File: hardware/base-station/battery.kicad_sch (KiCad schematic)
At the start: 24 parts, among them J2 USB4110GFA, U13 NTMD6N02R2G, U14 MAX17303G+, U5 BQ21040DBVR

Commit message: hardware: BOM-cost pass across all four boards
Component changes from a cross-board cost review. Per-board component cost
(USD @~100qty): rocket $86.21 -> $61.39, base station $35.91 -> $29.89, with
the LoRa daughterboard and GNSS SAM-M10Q board added to the shared BOM.

Memory architecture
  - Rocket: MR25H10 MRAM deleted; the log ring moves to in-package PSRAM.
    ESP32-S3 -> ESP32-S3RH2 (2 MB quad PSRAM, no in-package flash, same land
    pattern; SPICS1/GPIO26 was already unconnected on every board).
    Persistence across boots is knowingly given up.
  - Rocket NAND F35SQB004G-WWT -> GD5F2GQ5UEYIGR: pin- and footprint-identical
    (verified against the U11 land pattern), 4 Gbit -> 2 Gbit, $11.61 -> $3.50.
    Needs the 4096 -> 2048 B page migration in firmware.
  - Base station: dedicated log flash deleted entirely. It wrote one ~183 B CSV
    row per received packet at the 2 Hz downlink (~366 B/s, and only while a
    flight is active), so 256 MB was ~204 hours of headroom. The firmware
    already falls back to the existing SPIFFS partition, so this promotes a
    tested path rather than needing new code.
  - Boot flash W25Q64JVXGIQ -> W25Q128JVSIQ on all four positions: 16 MB for
    LESS money ($3.10 -> $2.21). SCHEMATIC ONLY - the boards still need
    "Update PCB from Schematic" plus re-placement, since SOIC-8 208mil is 2.2x
    the DFN's area. The DFN's 9th (exposed) pad was a redundant GND tie; pin 4
    is GND on all four, so nothing is lost.

Power
  - LoRa + GNSS keep TPS62913 (low-noise, RF rails). The rocket briefly moved
    to it and was REVERTED to TPS62152: the TPS62913 is forced-PWM with 5 mA
    quiescent, which would have raised the pad-idle floor ~6x against the
    light-sleep work.
  - Base load switch TPS22810 -> TPS22918 (identical footprint and pin order;
    pin 3 EN/UVLO -> ON is safe because it was driven as a plain enable).
    CT cap 10 nF -> 2.2 nF to match the rocket's ramp; R8 (QOD->VOUT) deleted.
  - LoRa gains a 7.5k S-CONF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
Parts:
- removed JP1: SolderJumper_2_Open, Jumper:SolderJumper-2_P1.3mm_Open_Pad1.0x1.5mm, symbol Jumper:SolderJumper_2_Open
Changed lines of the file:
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@@
 	)
 	(junction
-		(at 145.415 118.745)
-		(diameter 0)
-		(color 0 0 0 0)
-	)
-	(junction
 		(at 154.305 73.025)
 		(diameter 0)
@@
 	(wire
 		(pts
-			(xy 194.945 106.045) (xy 172.72 106.045)
-		)
-		(stroke
-			(width 0)
-			(type default)
-		)
-	)
-	(wire
-		(pts
 			(xy 107.315 157.48) (xy 84.455 157.48)
 		)
@@
 	(wire
 		(pts
-			(xy 67.31 118.745) (xy 145.415 118.745)
+			(xy 67.31 118.745) (xy 147.32 118.745)
 		)
 		(stroke
@@
 	(wire
 		(pts
-			(xy 145.415 118.745) (xy 147.32 118.745)
-		)
-		(stroke
-			(width 0)
-			(type default)
-		)
-	)
-	(wire
-		(pts
 			(xy 79.375 181.61) (xy 67.31 181.61)
 		)
@@
 	(wire
 		(pts
-			(xy 145.415 106.045) (xy 165.1 106.045)
-		)
-		(stroke
-			(width 0)
-			(type default)
-		)
-	)
-	(wire
-		(pts
-			(xy 194.945 106.045) (xy 194.945 118.745)
-		)
-		(stroke
-			(width 0)
-			(type default)
-		)
-	)
-	(wire
-		(pts
 			(xy 90.17 177.165) (xy 90.17 181.61)
 		)
@@
 	(wire
 		(pts
-			(xy 145.415 106.045) (xy 145.415 118.745)
-		)
-		(stroke
-			(width 0)
-			(type default)
-		)
-	)
-	(wire
-		(pts
 			(xy 154.305 50.165) (xy 167.64 50.165)
 		)
@@
 					(unit 1)
 				)
-			)
-		)
-	)
-	(symbol
-		(lib_id "Jumper:SolderJumper_2_Open")
-		(at 168.91 106.045 0)
-		(unit 1)
-		(body_style 1)
-		(exclude_from_sim no)
-		(in_bom no)
-		(on_board yes)
-		(in_pos_files yes)
-		(dnp no)
-		(fields_autoplaced yes)
-		(property "Reference" "JP1"
-			(at 168.91 99.695 0)
-			(show_name no)
-			(do_not_autoplace no)
-			(effects
-				(font
-					(size 1.27 1.27)
-				)
-			)
-		)
-		(property "Value" "SolderJumper_2_Open"
-			(at 168.91 102.235 0)
-			(show_name no)
-			(do_not_autoplace no)
-			(effects
-				(font
-					(size 1.27 1.27)
-				)
-			)
-		)
-		(property "Footprint" "Jumper:SolderJumper-2_P1.3mm_Open_Pad1.0x1.5mm"
-			(at 168.91 106.045 0)
-			(hide yes)
-			(show_name no)
-			(do_not_autoplace no)
-			(effects
-				(font
-					(size 1.27 1.27)
-				)
-			)
-		)
-		(property "Datasheet" ""
-			(at 168.91 106.045 0)
-			(hide yes)
-			(show_name no)
-			(do_not_autoplace no)
-			(effects
-				(font
-					(size 1.27 1.27)
-				)
-			)
-		)
-		(property "Description" "Solder Jumper, 2-pole, open"
-			(at 168.91 106.045 0)
-			(hide yes)
-			(show_name no)
-			(do_not_autoplace no)
-			(effects
-				(font
-					(size 1.27 1.27)
-				)
-			)
-		)
-		(pin "1"
-		)
-		(pin "2"
-		)
-		(instances
-			(project "base-station"
-				(path "/d2421514-d142-4c71-ac69-48d30c1a771f/2379f198-28b9-4984-b470-63cb7f5b1a0e"
-					(reference "JP1")
-					(unit 1)
-				)

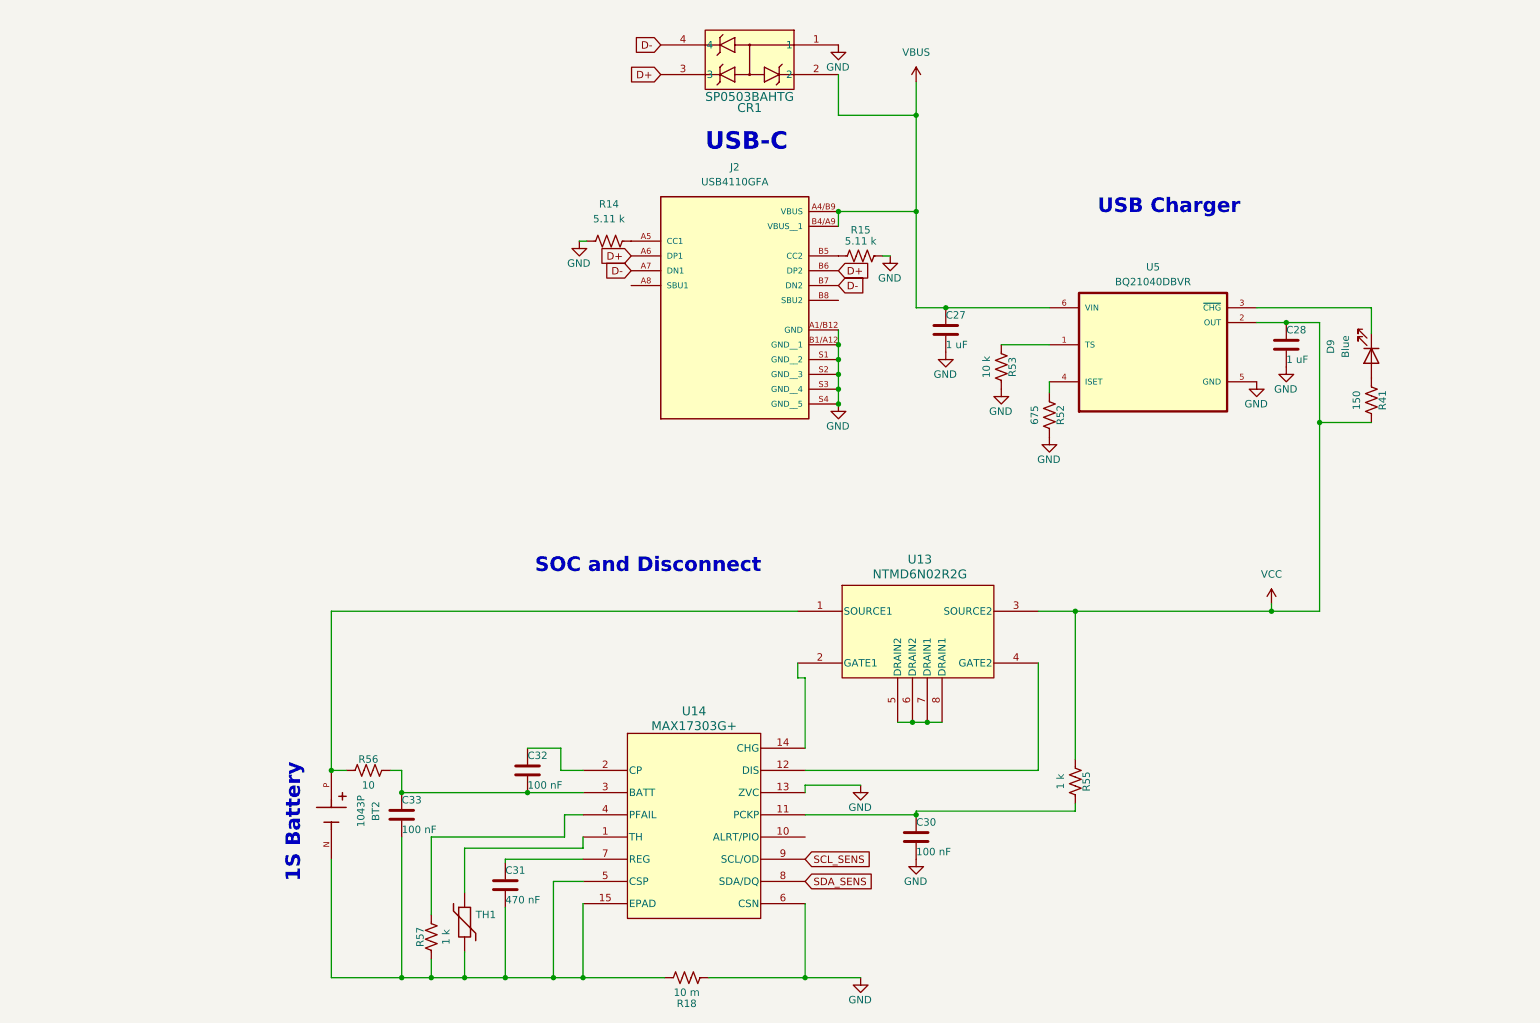
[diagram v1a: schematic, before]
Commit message: hardware: battery protection, boost swap, and a capacitor voltage audit
Base station power chain, all verified against exported netlists:

- Protection: MAX17303G+ gauge/protector and its NTMD6N02R2G FET pair
  replaced by DW01A + 2x FS8205A. The MAX17303 had no firmware driver and
  the board never had a working coulomb counter, so state of charge already
  came from the voltage curve in bs_battery_soc.h; it now reads a 1M/1M
  divider on GPIO1. The FETs move from the positive rail to the negative
  one because the DW01A has no charge pump, so board ground is now P-,
  separated from the cell's B- by the FET stack. Two FS8205A in parallel
  put the 150 mV overcurrent trip at ~4.8-6.0 A instead of ~2.4-3.0 A.
  TH1 moves onto the BQ21040's TS pin, replacing a fixed 10k that had been
  defeating thermal charge cutoff.

- V_LORA retargeted 7.49 V -> 4.95 V and LM5157QRTERQ1 -> TPS61023DRLR.
  Nothing needed 7.4 V (everything downstream is 3.3 V behind the
  TPS62913), while an RFD868x-class radio is 5 V nominal with a 6 V
  absolute maximum, so the old rail put it permanently out of reach. Being
  synchronous and internally compensated also dropped D2, C35-C38 and R10.
  Inductor stays the fleet 2.2 uH: inside TI's 0.37-2.9 uH range and the
  only value meeting their ripple-under-40%-of-average guidance at load.

- Keystone 1043P holder -> MYOUNG BH-18650-A5BJ001-2D. Terminal pitch
  72.30 vs 72.22 mm, so the battery nets did not move; BT2 is rotated 180
  degrees because this part's positive end is mirrored.

Across all four boards:

- Every crystal was mis-loaded. 32.768 kHz parts saw ~9 pF against a 6 pF
  spec and the 40 MHz saw 12.5 pF against 10 pF, both pulling slow. Moved
  to Seiko SC-32S (12.5 pF) with 22 pF load caps, and the 40 MHz caps to
  18 pF. The tolerance being paid for had been swamped several times over.

- Capacitor voltage audit, new Min V rating column in the BOM. Three parts
  were operating outside their rating on 8.4 V rails: 47 uF and 100 u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
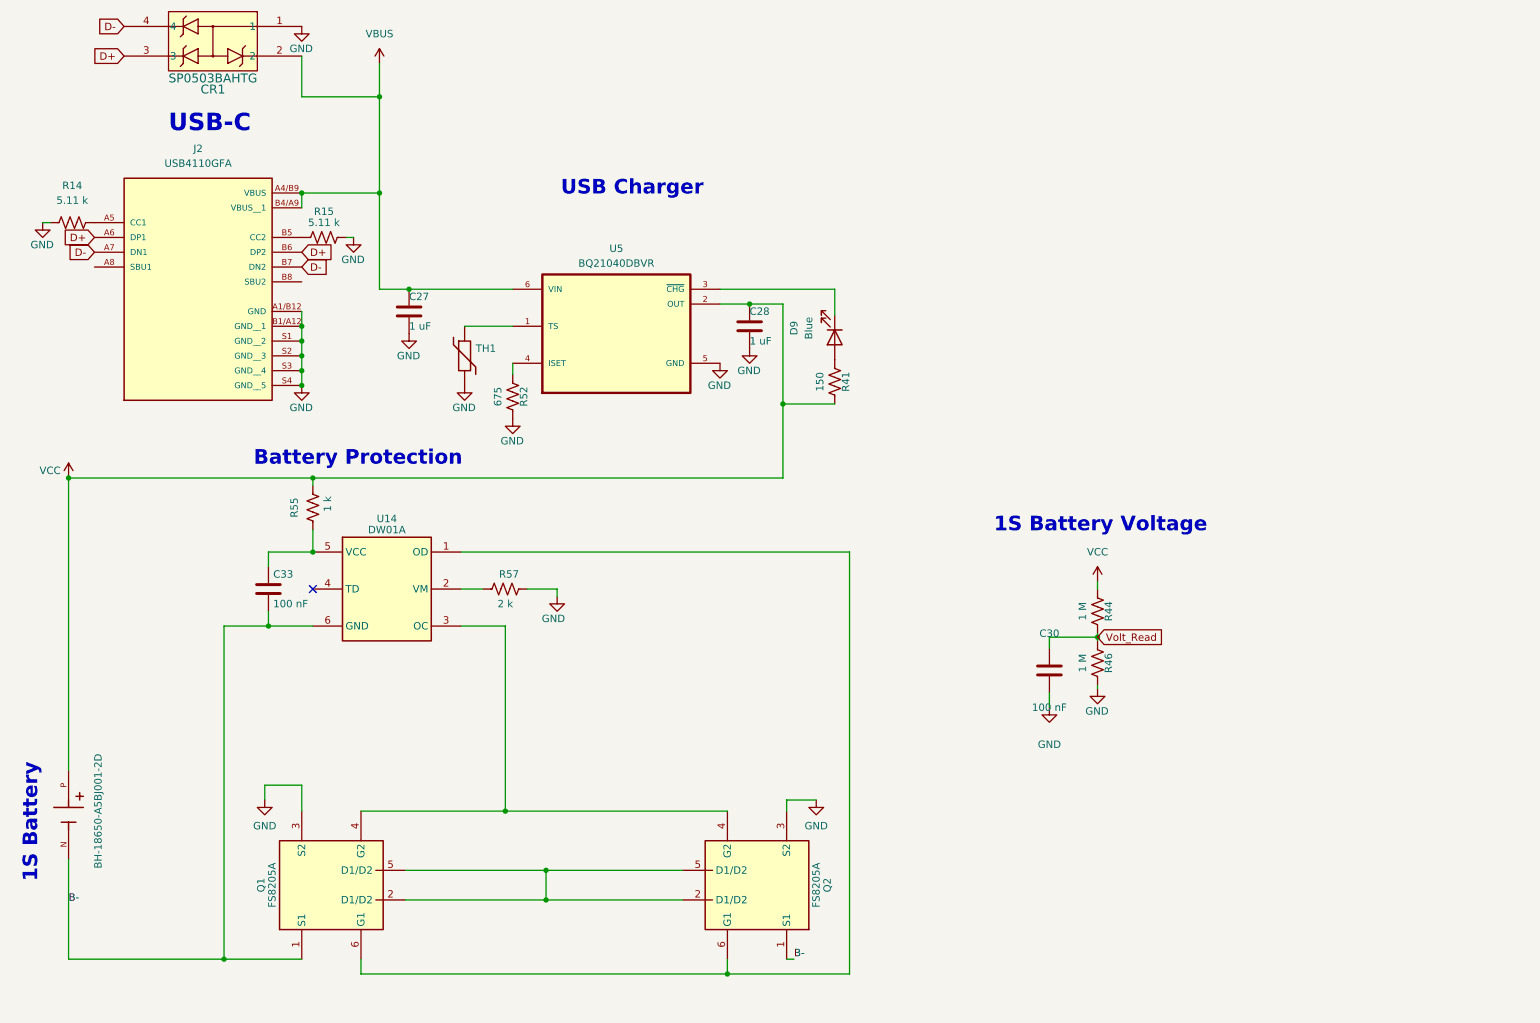
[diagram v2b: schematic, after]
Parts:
- removed C31: 470 nF, Capacitor_SMD:C_0402_1005Metric, symbol Device:C
- removed C32: 100 nF, Capacitor_SMD:C_0402_1005Metric, symbol Device:C
- removed R18: 10 m, Resistor_SMD:R_1206_3216Metric, symbol Device:R_US
- removed R53: 10 k, Resistor_SMD:R_0402_1005Metric, symbol Device:R_US
- removed R56: 10, Resistor_SMD:R_0402_1005Metric, symbol Device:R_US
- removed U13: NTMD6N02R2G, SOIC8_4X5_ONS, symbol Custom:NTMD6N02R2G
- removed U14: MAX17303G+, 21-0137I_T1433-2_MXM, symbol Custom:MAX17303G+
- added Q1, Q2: FS8205A, Package_TO_SOT_SMD:SOT-23-6, symbol Custom:FS8205A
- added R44, R46: 1 M, Resistor_SMD:R_0402_1005Metric, symbol Device:R_US
- added U14: DW01A, Package_TO_SOT_SMD:SOT-23-6, symbol Custom:DW01A
- BT2: value 1043P -> BH-18650-A5BJ001-2D; footprint Footprints:BAT_1043P -> Footprints:BAT_BH-18650-A5BJ001-2D; symbol Custom:1043P -> Custom:BH-18650-A5BJ001-2D; Check_prices https://www.snapeda.com/parts/1043P/Keystone/view-part/?ref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 -> (none); DigiKey_Part_Number 36-1043P-ND -> (none); LCSC_Part_Number (none) -> C19184083; MANUFACTURER Keystone -> MYOUNG; MAXIMUM_PACKAGE_HEIGHT 15.11mm -> (none); MF Keystone Electronics -> MYOUNG; MP 1043P -> BH-18650-A5BJ001-2D; SNAPEDA_PN 1043P -> BH-18650-A5BJ001-2D; SnapEDA_Link https://www.snapeda.com/parts/1043P/Keystone/view-part/?ref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 -> (none)
- R57: value 1 k -> 2 k
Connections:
- net GND: now also R57.2, TH1.2, Q1.3 (S2), Q2.3 (S2), R46.2
- net VCC: now also BT2.P, R44.1
- net at C33.1: now also R55.2, U14.5 (VCC)
- net at TH1.1: now also U5.1 (TS)
- net B-: now reaches BT2.N, C33.2
- net B-: now also Q1.1 (S1), Q2.1 (S1), U14.6 (GND); no longer R57.1, TH1.2
- net Volt_Read: now reaches C30.1
- net Volt_Read: now also R44.2, R46.1; no longer R55.2
- new net: R57.1, U14.2 (VM)
- new net: Q1.2 (D1/D2), Q1.5 (D1/D2), Q2.2 (D1/D2), Q2.5 (D1/D2)
- new net: Q1.4 (G2), Q2.4 (G2), U14.3 (OC)
- new net: Q1.6 (G1), Q2.6 (G1), U14.1 (OD)
- no-connect marks 0 -> 1
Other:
- note added: "1S Battery Voltage"
- note added: "Battery Protection"
- note removed: "SOC and Disconnect"
- moved on the sheet: C27, C28, CR1, D9, J2, R14, R15, R41, R52, TH1, U5

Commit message: hardware: add a third FS8205A to the base-station protection stack
The DW01A senses its 150 mV +/-30 mV overcurrent threshold across the
whole FET stack, so the trip point is the stack resistance. Two FS8205A
(31.5 mOhm) trip at 2.72 A at the hot corner - only 1.09x an RFD868x's
~2.5 A peak, close enough to nuisance-trip. A third (21.0 mOhm) moves
that to 4.08 A, 1.63x.

Three rather than four: a fourth would put the cold-typical trip at
~9.5 A, at or past an 18650's continuous rating, where it stops
protecting the cell.

Nothing is given up on short-circuit. The DW01A's VSHORT is specified
0.82/1.36/1.75 V min/typ/max, and against the 1.75 V corner the fast
path already fails at two FETs for every realistic cell resistance - a
short is caught by the 150 mV overcurrent path at 7 ms either way.

Q3 attaches by label rather than by extending the existing rails, so the
three previously auto-named nets are now PROT_DRAIN, PROT_OD and PROT_OC.
Net membership is otherwise byte-identical: verified against exported
netlists before and after, 103 nets, every pre-existing net unchanged.
ERC goes 500 -> 501, the one addition being the lib_symbol_mismatch that
every other GND symbol on the sheet already carries.

Also corrects two stale library descriptions: the FS8205A said "TWO of
these" with a ~4.8-6.0 A trip that was computed from the typical rather
than the minimum threshold, and the DW01A said "short-circuit 1.2 V"
against a real 0.82-1.75 V spread. Both now record the vendor-spread
caution - Slkor's DW01A is 4.3 V +/-80 mV over temperature, whose low
corner sits under the BQ21040's 4.23 V regulation maximum.

Includes R55 1 k -> 100 R, the DW01A datasheet's own value.

Co-Authored-By: Claude Opus 5 <noreply@anthropic.com>
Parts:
- added Q3: FS8205A, Package_TO_SOT_SMD:SOT-23-6, symbol Custom:FS8205A
- R55: value 1 k -> 100
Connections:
- net B-: now also Q3.1 (S1)
- net GND: now also Q3.3 (S2)
- net PROT_DRAIN: now reaches Q1.2 (D1/D2), Q1.5 (D1/D2), Q2.2 (D1/D2), Q2.5 (D1/D2)
- net PROT_DRAIN: now also Q3.2 (D1/D2), Q3.5 (D1/D2)
- net PROT_OC: now reaches Q1.4 (G2), Q2.4 (G2), U14.3 (OC)
- net PROT_OC: now also Q3.4 (G2)
- net PROT_OD: now reaches Q1.6 (G1), Q2.6 (G1), U14.1 (OD)
- net PROT_OD: now also Q3.6 (G1)
